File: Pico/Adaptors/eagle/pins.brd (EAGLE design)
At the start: 26 x 20.6 mm, 5 parts, among them J1 JST-2P-SMD-PW-3410050P1

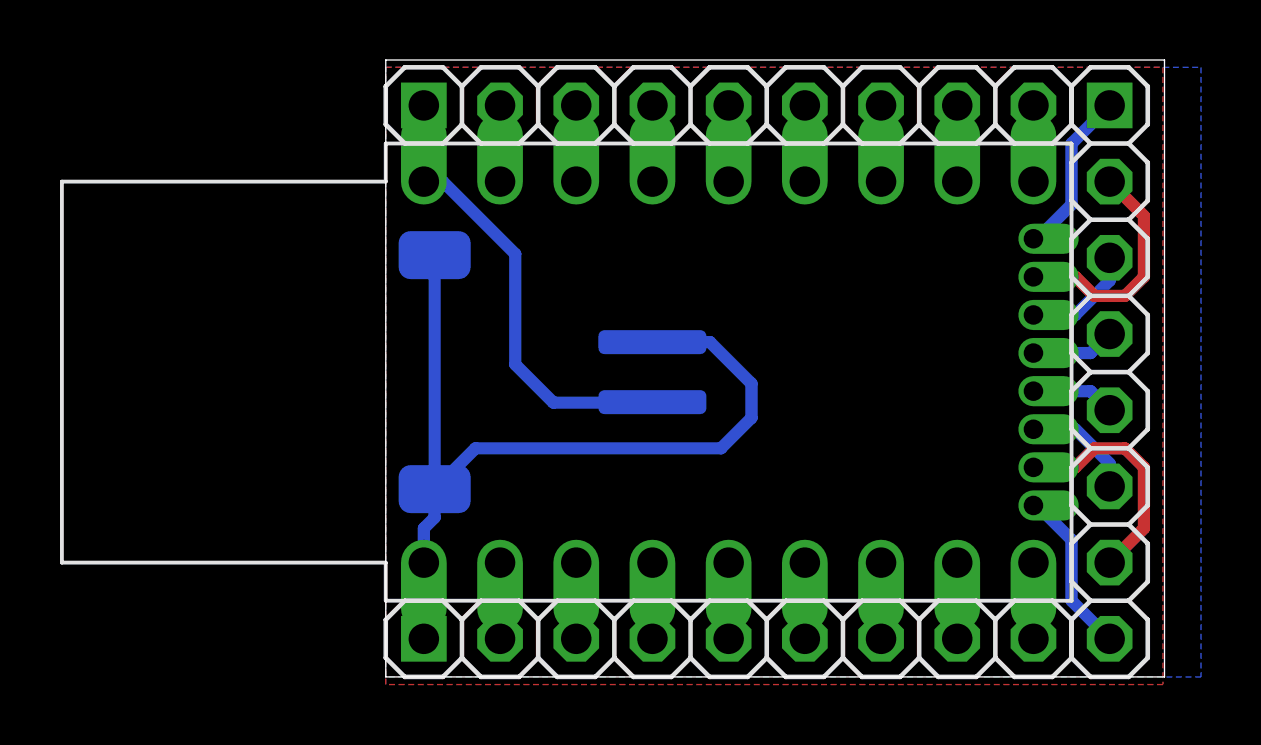
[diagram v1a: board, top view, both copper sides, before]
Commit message: Added battery charger pads to proto headers
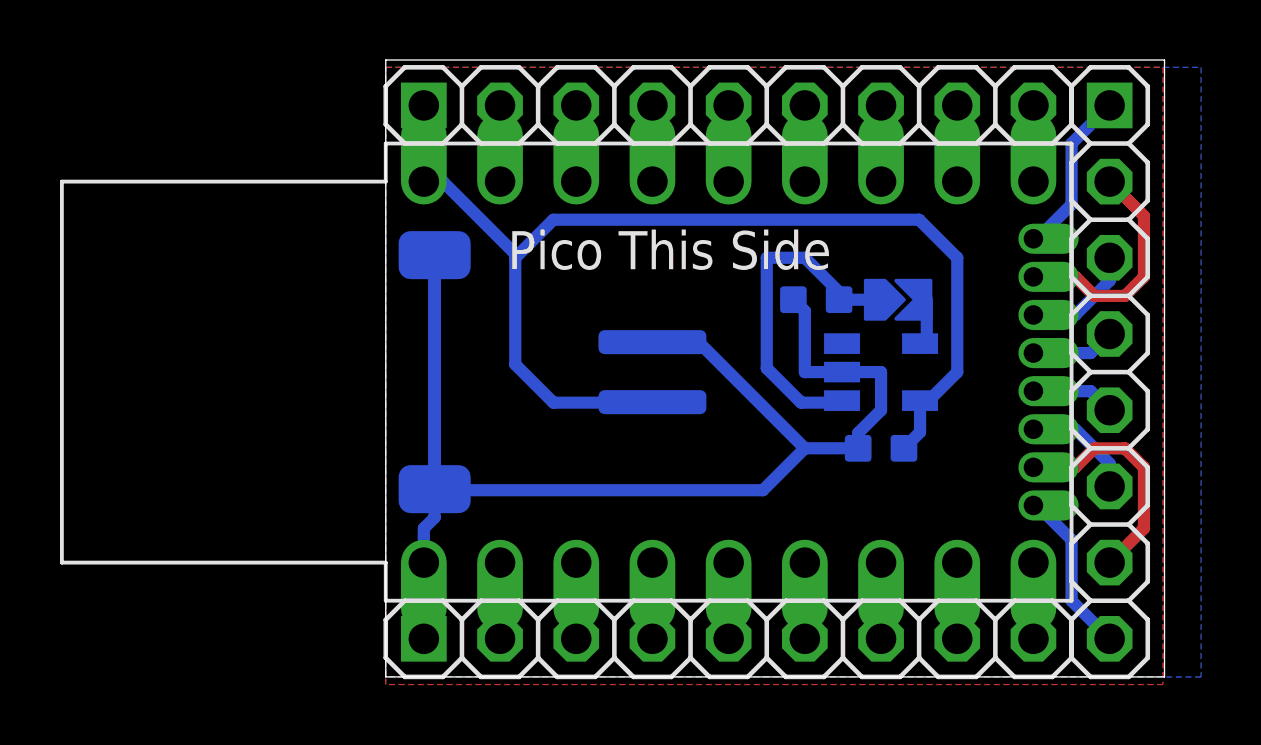
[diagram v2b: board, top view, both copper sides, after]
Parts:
- added C1, C2: 100nF, OPL5:C0603
- added U$4: SOLDERJUMPER, solder_jumper:SOLDERJUMPER
- added U3: MAX1551, template:SOT23-5
- J2: value JST-2P-SMD-PW-3410050P1 -> (none)
- renumbered J1 to J2
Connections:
- removed net 5V: JP4.2, U$1.5V
- new net N$15: U$4.P$1, U3.4
- new net VIN: C2.1, JP4.2, U$1.5V, U$4.P$2, U3.1
- net BAT: now also C1.1, U3.5
- net GND: now also C1.2, C2.2, U3.2
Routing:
- net BAT: track 15.4 -> 38.4 mm
- net GND: track 29.5 -> 49.9 mm
- net VIN: track 0.00 -> 13.4 mm
- net 5V: track 2.54 -> 0.00 mm
- net N$15: track 0.00 -> 1.56 mm
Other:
- board text added: "Pico This Side"
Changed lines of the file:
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@@
 <layer number="111" name="111" color="7" fill="1" visible="no" active="no"/>
 <layer number="112" name="tSilk" color="7" fill="1" visible="no" active="no"/>
+<layer number="113" name="IDFDebug" color="7" fill="1" visible="yes" active="yes"/>
 <layer number="116" name="Patch_BOT" color="9" fill="4" visible="no" active="no"/>
 <layer number="118" name="Rect_Pads" color="7" fill="1" visible="no" active="no"/>
@@
 <layer number="223" name="223bmp" color="24" fill="1" visible="no" active="no"/>
 <layer number="224" name="224bmp" color="25" fill="1" visible="no" active="no"/>
+<layer number="225" name="225bmp" color="7" fill="1" visible="yes" active="yes"/>
+<layer number="226" name="226bmp" color="7" fill="1" visible="yes" active="yes"/>
+<layer number="227" name="227bmp" color="7" fill="1" visible="yes" active="yes"/>
+<layer number="228" name="228bmp" color="7" fill="1" visible="yes" active="yes"/>
+<layer number="230" name="230bmp" color="7" fill="1" visible="no" active="yes"/>
 <layer number="248" name="Housing" color="7" fill="1" visible="no" active="no"/>
 <layer number="249" name="Edge" color="7" fill="1" visible="no" active="no"/>
@@
 <wire x1="25.959" y1="20.564" x2="0" y2="20.564" width="0" layer="20"/>
 <wire x1="0" y1="20.564" x2="0" y2="0" width="0" layer="20"/>
+<text x="4.064" y="13.589" size="1.27" layer="25">Pico This Side</text>
 </plain>
 <attributes>
@@
 <classes>
 <class number="0" name="default" width="0.3048" drill="0">
+</class>
+<class number="1" name="power" width="0.4064" drill="0">
 </class>
 </classes>
@@
 <attribute name="VALUE" x="0" y="-1.905" size="1.27" layer="27"/>
 </element>
-<element name="J1" library="OPL Eagle Library" package="2P-SMD-2.0-90D" value="JST-2P-SMD-PW-3410050P1" x="3.81" y="10.16" rot="MR90"/>
+<element name="J2" library="OPL Eagle Library" package="2P-SMD-2.0-90D" value="" x="3.81" y="10.16" smashed="yes" rot="MR90">
+<attribute name="VALUE" x="3.81" y="8.255" size="0.635" layer="28" ratio="10" rot="MR90"/>
+</element>
+<element name="U3" library="template" package="SOT23-5" value="MAX1551" x="16.51" y="10.16" smashed="yes" rot="MR90">
+<attribute name="VALUE" x="18.6055" y="9.3345" size="0.635" layer="28" ratio="10" rot="MR90"/>
+</element>
+<element name="C2" library="OPL5" package="C0603" value="100nF" x="14.351" y="12.573" smashed="yes" rot="MR0">
+<attribute name="NAME" x="15.875" y="13.589" size="0.889" layer="26" ratio="11" rot="MR0"/>
+<attribute name="VALUE" x="13.97" y="13.6525" size="0.508" layer="28" ratio="10" rot="MR0"/>
+</element>
+<element name="C1" library="OPL5" package="C0603" value="100nF" x="16.51" y="7.62" smashed="yes" rot="MR0">
+<attribute name="NAME" x="18.288" y="5.715" size="0.889" layer="26" ratio="11" rot="MR0"/>
+<attribute name="VALUE" x="16.637" y="6.0325" size="0.508" layer="28" ratio="10" rot="MR0"/>
+</element>
+<element name="U$4" library="solder_jumper" package="SOLDERJUMPER" value="SOLDERJUMPER" x="17.272" y="12.573" rot="MR180"/>
 </elements>
 <signals>
@@
 <wire x1="25.273" y1="6.985" x2="25.273" y2="4.953" width="0.4064" layer="1"/>
 <wire x1="25.273" y1="4.953" x2="24.13" y2="3.81" width="0.4064" layer="1"/>
-</signal>
-<signal name="5V">
-<contactref element="U$1" pad="5V"/>
-<contactref element="JP4" pad="2"/>
-<wire x1="3.81" y1="3.81" x2="3.81" y2="1.27" width="1.016" layer="16"/>
 </signal>
 <signal name="GND">
@@
 <vertex x="0" y="0"/>
 </polygon>
-<contactref element="J1" pad="-"/>
-<contactref element="J1" pad="3"/>
-<contactref element="J1" pad="4"/>
-<wire x1="8.89" y1="11.16" x2="10.811" y2="11.16" width="0.4064" layer="16"/>
-<wire x1="10.811" y1="11.16" x2="12.192" y2="9.779" width="0.4064" layer="16"/>
-<wire x1="12.192" y1="9.779" x2="12.192" y2="8.636" width="0.4064" layer="16"/>
-<wire x1="12.192" y1="8.636" x2="11.176" y2="7.62" width="0.4064" layer="16"/>
-<wire x1="11.176" y1="7.62" x2="2.989" y2="7.62" width="0.4064" layer="16"/>
-<wire x1="2.989" y1="7.62" x2="1.629" y2="6.26" width="0.4064" layer="16"/>
-<wire x1="1.629" y1="6.26" x2="1.629" y2="14.06" width="0.4064" layer="16"/>
-<wire x1="1.629" y1="6.26" x2="1.629" y2="5.312" width="0.4064" layer="16"/>
 <wire x1="1.629" y1="5.312" x2="1.27" y2="4.953" width="0.4064" layer="16"/>
 <wire x1="1.27" y1="4.953" x2="1.27" y2="3.81" width="0.4064" layer="16"/>
+<contactref element="U3" pad="2"/>
+<contactref element="C1" pad="2"/>
+<contactref element="C2" pad="2"/>
+<contactref element="J2" pad="-"/>
+<contactref element="J2" pad="3"/>
+<contactref element="J2" pad="4"/>
+<wire x1="15.748" y1="7.62" x2="15.748" y2="8.128" width="0.4064" layer="16"/>
+<wire x1="15.748" y1="8.128" x2="16.51" y2="8.89" width="0.4064" layer="16"/>
+<wire x1="16.51" y1="8.89" x2="16.51" y2="10.16" width="0.4064" layer="16"/>
+<wire x1="16.51" y1="10.16" x2="15.2099" y2="10.16" width="0.4064" layer="16"/>
+<wire x1="15.2099" y1="10.16" x2="13.97" y2="10.16" width="0.4064" layer="16"/>
+<wire x1="13.97" y1="10.16" x2="13.97" y2="12.192" width="0.4064" layer="16"/>
+<wire x1="13.97" y1="12.192" x2="13.589" y2="12.573" width="0.4064" layer="16"/>
+<wire x1="8.89" y1="11.16" x2="10.43" y2="11.16" width="0.4064" layer="16"/>
+<wire x1="10.43" y1="11.16" x2="13.97" y2="7.62" width="0.4064" layer="16"/>
+<wire x1="13.97" y1="7.62" x2="15.748" y2="7.62" width="0.4064" layer="16"/>
+<wire x1="1.629" y1="5.312" x2="1.629" y2="6.26" width="0.4064" layer="16"/>
+<wire x1="1.629" y1="6.26" x2="1.629" y2="14.06" width="0.4064" layer="16"/>
+<wire x1="1.629" y1="14.06" x2="1.629" y2="6.372" width="0.4064" layer="16"/>
+<wire x1="1.629" y1="6.372" x2="1.778" y2="6.223" width="0.4064" layer="16"/>
+<wire x1="1.778" y1="6.223" x2="12.573" y2="6.223" width="0.4064" layer="16"/>
+<wire x1="12.573" y1="6.223" x2="13.97" y2="7.62" width="0.4064" layer="16"/>
 </signal>
 <signal name="N$9">
@@
 <contactref element="JP3" pad="1"/>
 <wire x1="1.27" y1="16.51" x2="1.27" y2="19.05" width="1.016" layer="16"/>
-<contactref element="J1" pad="+"/>
 <wire x1="1.27" y1="16.51" x2="1.905" y2="16.51" width="0.4064" layer="16"/>
 <wire x1="1.905" y1="16.51" x2="4.318" y2="14.097" width="0.4064" layer="16"/>
-<wire x1="4.318" y1="14.097" x2="4.318" y2="10.414" width="0.4064" layer="16"/>
+<wire x1="4.318" y1="14.097" x2="4.318" y2="13.97" width="0.4064" layer="16"/>
+<wire x1="4.318" y1="13.97" x2="4.318" y2="10.414" width="0.4064" layer="16"/>
 <wire x1="4.318" y1="10.414" x2="5.588" y2="9.144" width="0.4064" layer="16"/>
+<contactref element="U3" pad="5"/>
+<contactref element="C1" pad="1"/>
+<contactref element="J2" pad="+"/>
+<wire x1="17.8101" y1="9.21" x2="17.8101" y2="8.1581" width="0.4064" layer="16"/>
+<wire x1="17.8101" y1="8.1581" x2="17.272" y2="7.62" width="0.4064" layer="16"/>
 <wire x1="5.588" y1="9.144" x2="8.874" y2="9.144" width="0.4064" layer="16"/>
 <wire x1="8.874" y1="9.144" x2="8.89" y2="9.16" width="0.4064" layer="16"/>
+<wire x1="17.8101" y1="9.21" x2="18.1" y2="9.21" width="0.4064" layer="16"/>
+<wire x1="18.1" y1="9.21" x2="19.05" y2="10.16" width="0.4064" layer="16"/>
+<wire x1="19.05" y1="10.16" x2="19.05" y2="13.97" width="0.4064" layer="16"/>
+<wire x1="19.05" y1="13.97" x2="17.78" y2="15.24" width="0.4064" layer="16"/>
+<wire x1="17.78" y1="15.24" x2="5.588" y2="15.24" width="0.4064" layer="16"/>
+<wire x1="5.588" y1="15.24" x2="4.318" y2="13.97" width="0.4064" layer="16"/>
 </signal>
 <signal name="N$16">
@@
 <wire x1="22.86" y1="17.78" x2="24.13" y2="19.05" width="0.4064" layer="16"/>
 </signal>
+<signal name="VIN" class="1">
+<contactref element="U3" pad="1"/>
+<contactref element="C2" pad="1"/>
+<contactref element="U$4" pad="P$2"/>
+<contactref element="U$1" pad="5V"/>
+<contactref element="JP4" pad="2"/>
+<wire x1="3.81" y1="3.81" x2="3.81" y2="1.27" width="1.016" layer="16"/>
+<wire x1="3.81" y1="1.27" x2="15.2099" y2="9.21" width="0" layer="19" extent="1-1"/>
+<wire x1="15.113" y1="12.573" x2="16.129" y2="12.573" width="0.4064" layer="16"/>
+<wire x1="15.113" y1="12.573" x2="15.113" y2="12.827" width="0.4064" layer="16"/>
+<wire x1="15.113" y1="12.827" x2="13.97" y2="13.97" width="0.4064" layer="16"/>
+<wire x1="13.97" y1="13.97" x2="12.7" y2="13.97" width="0.4064" layer="16"/>
+<wire x1="12.7" y1="13.97" x2="12.7" y2="10.287" width="0.4064" layer="16"/>
+<wire x1="12.7" y1="10.287" x2="13.843" y2="9.144" width="0.4064" layer="16"/>
+<wire x1="13.843" y1="9.144" x2="15.1439" y2="9.144" width="0.4064" layer="16"/>
+<wire x1="15.1439" y1="9.144" x2="15.2099" y2="9.21" width="0.4064" layer="16"/>
+</signal>
+<signal name="N$15">
+<contactref element="U3" pad="4"/>
+<contactref element="U$4" pad="P$1"/>
+<wire x1="18.034" y1="12.573" x2="18.034" y2="11.3339" width="0.4064" layer="16"/>
+<wire x1="18.034" y1="11.3339" x2="17.8101" y2="11.11" width="0.4064" layer="16"/>
+</signal>
 </signals>
